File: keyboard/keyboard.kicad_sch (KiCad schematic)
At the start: 69 parts, among them J1 TYPE-C-31-M-12, J2 Conn_01x03_Socket, J3 Conn_01x02_Pin, J4 AudioJack4, J5 Conn_02x06_Top_Bottom, J6 Conn_02x06_Top_Bottom, J7 Conn_01x05_Socket, SW1 SW_MEC_5G, SW10 SW_MEC_5G, SW11 SW_MEC_5G, SW12 SW_MEC_5G, SW13 SW_MEC_5G, SW14 SW_MEC_5G, SW15 SW_MEC_5G, SW16 SW_key, SW17 SW_MEC_5G, SW18 SW_MEC_5G, SW2 SW_MEC_5G, SW3 SW_MEC_5G, SW4 SW_MEC_5G, SW5 SW_MEC_5G, SW6 SW_MEC_5G, SW7 SW_MEC_5G, SW8 SW_MEC_5G, SW9 SW_MEC_5G, U1 RP2040, U2 NCP1117-3.3_SOT223, U3 W25Q128JVS, Y1 ABLS-12.000MHZ-B4-T

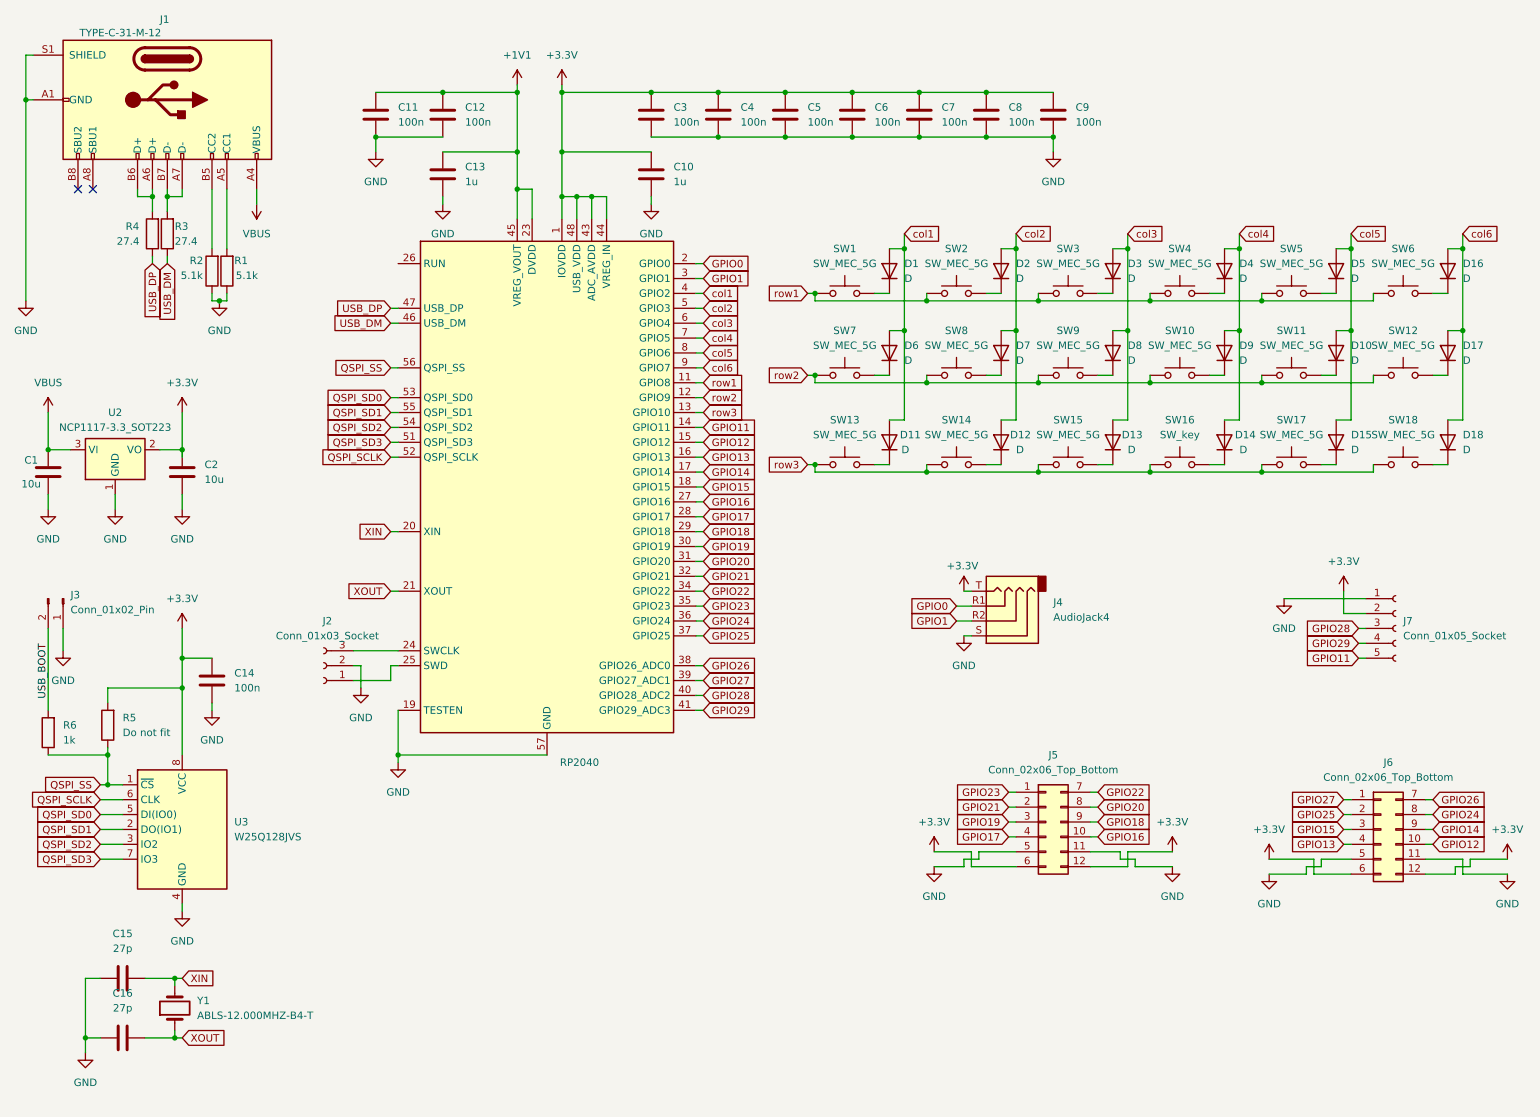
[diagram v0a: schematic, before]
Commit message: add footprints and New design as BOARD
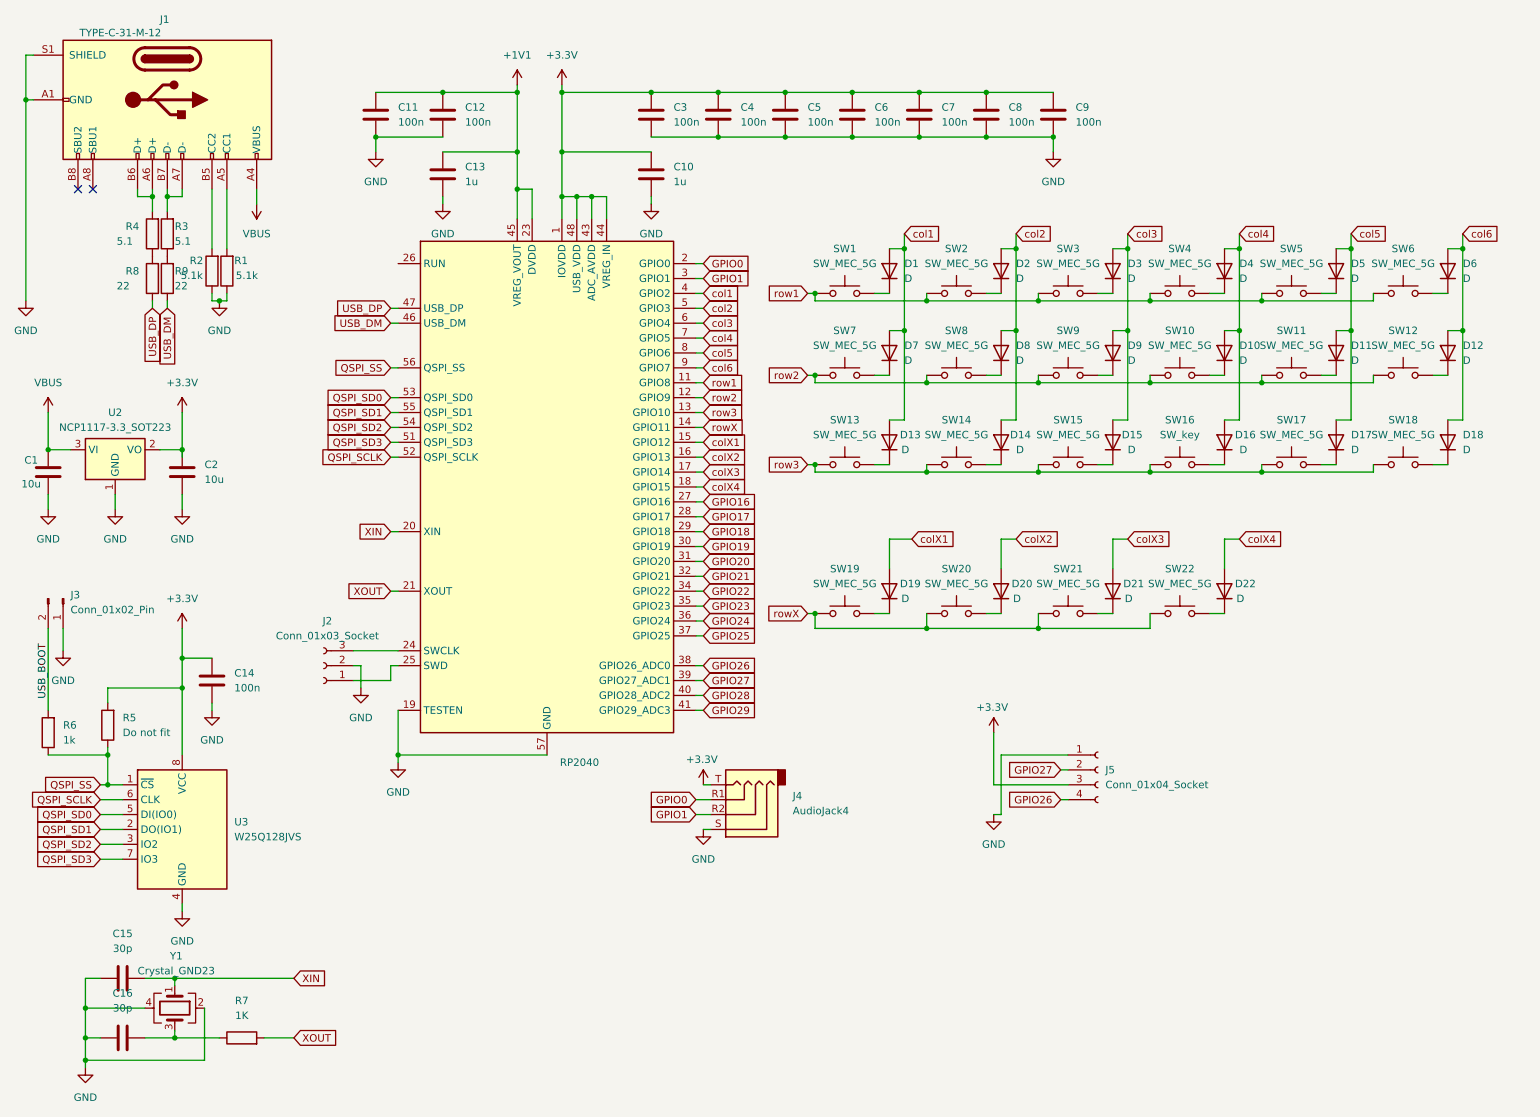
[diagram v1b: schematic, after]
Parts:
- removed J5, J6: Conn_02x06_Top_Bottom, Connector_PinSocket_2.54mm:PinSocket_2x06_P2.54mm_Horizontal, symbol Connector_Generic:Conn_02x06_Top_Bottom
- removed J7: Conn_01x05_Socket, Connector_PinSocket_2.54mm:PinSocket_1x05_P2.54mm_Horizontal, symbol Connector:Conn_01x05_Socket
- removed Y1: ABLS-12.000MHZ-B4-T, kicad:XTAL_ABLS-27.120MHZ-B4-F-T, symbol Device:Crystal
- added D19, D20, D21, D22: D, Diode_SMD:D_SOD-123, symbol Device:D
- added J5: Conn_01x04_Socket, footprint:JT8P-3.2T- -1-16Y, symbol Connector:Conn_01x04_Socket
- added R7: 1K, Resistor_SMD:R_0603_1608Metric, symbol Device:R
- added R8, R9: 22, Resistor_SMD:R_0603_1608Metric, symbol Device:R
- added SW19, SW20, SW21, SW22: SW_MEC_5G, Button_Switch_Keyboard:SW_Cherry_MX_1.00u_PCB, symbol sw_key:SW_MEC_5G_1
- added Y1: Crystal_GND23, Crystal:Crystal_SMD_3225-4Pin_3.2x2.5mm, symbol Device:Crystal_GND24
- C15, C16: value 27p -> 30p; footprint Capacitor_SMD:C_0402_1005Metric -> Capacitor_SMD:C_0603_1608Metric
- J1: footprint Connector_USB:USB_C_Receptacle_G-Switch_GT-USB-7025 -> Connector_USB:USB_C_Receptacle_HRO_TYPE-C-31-M-12
- J2: footprint Connector_PinSocket_2.54mm:PinSocket_1x03_P2.54mm_Horizontal -> footprint:PinSocket_1x03_P2.54mm_Horizontal
- J3: footprint Connector_PinHeader_2.54mm:PinHeader_1x02_P2.54mm_Horizontal -> footprint:PinHeader_1x02_P2.54mm_Horizontal
- J4: footprint Connector_Audio:Jack_3.5mm_KoreanHropartsElec_PJ-320D-4A_Horizontal -> footprint:MJ-4PP-9
- R1, R2, R6: footprint Resistor_SMD:R_1206_3216Metric -> Resistor_SMD:R_0603_1608Metric
- R3, R4: value 27.4 -> 5.1; footprint Resistor_SMD:R_1206_3216Metric -> Resistor_SMD:R_0603_1608Metric
- U3: footprint Package_SO:SOIC-8_5.23x5.23mm_P1.27mm -> footprint:SOIC_128JVSIM_WIN
- renumbered D9 to D10, D10 to D11, D17 to D12, D11 to D13, D12 to D14, D13 to D15, D14 to D16, D15 to D17, D16 to D6, D6 to D7, D7 to D8, D8 to D9
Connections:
- net +3.3V: now also J5.3 (Pin_3)
- net GND: now also J5.1 (Pin_1), Y1.2, Y1.4
- net GPIO26: now also J5.4 (Pin_4)
- net GPIO27: now also J5.2 (Pin_2)
- net USB_DM: now also R9.1; no longer R3.1
- net USB_DP: now also R8.1; no longer R4.1
- net XIN: now also Y1.1
- net XOUT: now also R7.2; no longer C16.2
- net GPIO11 renamed rowX
- net rowX: now also SW19.1 (A), SW20.1 (A), SW21.1 (A), SW22.1 (A)
- net GPIO12 renamed colX1
- net colX1: now also D19.2 (A)
- net GPIO13 renamed colX2
- net colX2: now also D20.2 (A)
- net GPIO14 renamed colX3
- net colX3: now also D21.2 (A)
- net GPIO15 renamed colX4
- net colX4: now also D22.2 (A)
- new net: D22.1 (K), SW22.2 (B)
- new net: D19.1 (K), SW19.2 (B)
- new net: C16.2, R7.1, Y1.3
- new net: D21.1 (K), SW21.2 (B)
- new net: R3.1, R9.2
- new net: R4.1, R8.2
- new net: D20.1 (K), SW20.2 (B)
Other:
- moved on the sheet: J4
